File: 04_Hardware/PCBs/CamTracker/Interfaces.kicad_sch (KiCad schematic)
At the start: 58 parts, among them J7 22-28-4044, J8 22-28-4044, Q1 BC817-40,215, Q2 BC817-40,215, Q3 BC817-40,215, Q4 BC817-40,215, Q5 BC817-40,215, Q6 BC817-40,215, Q7 BC817-40,215, Q8 BC817-40,215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

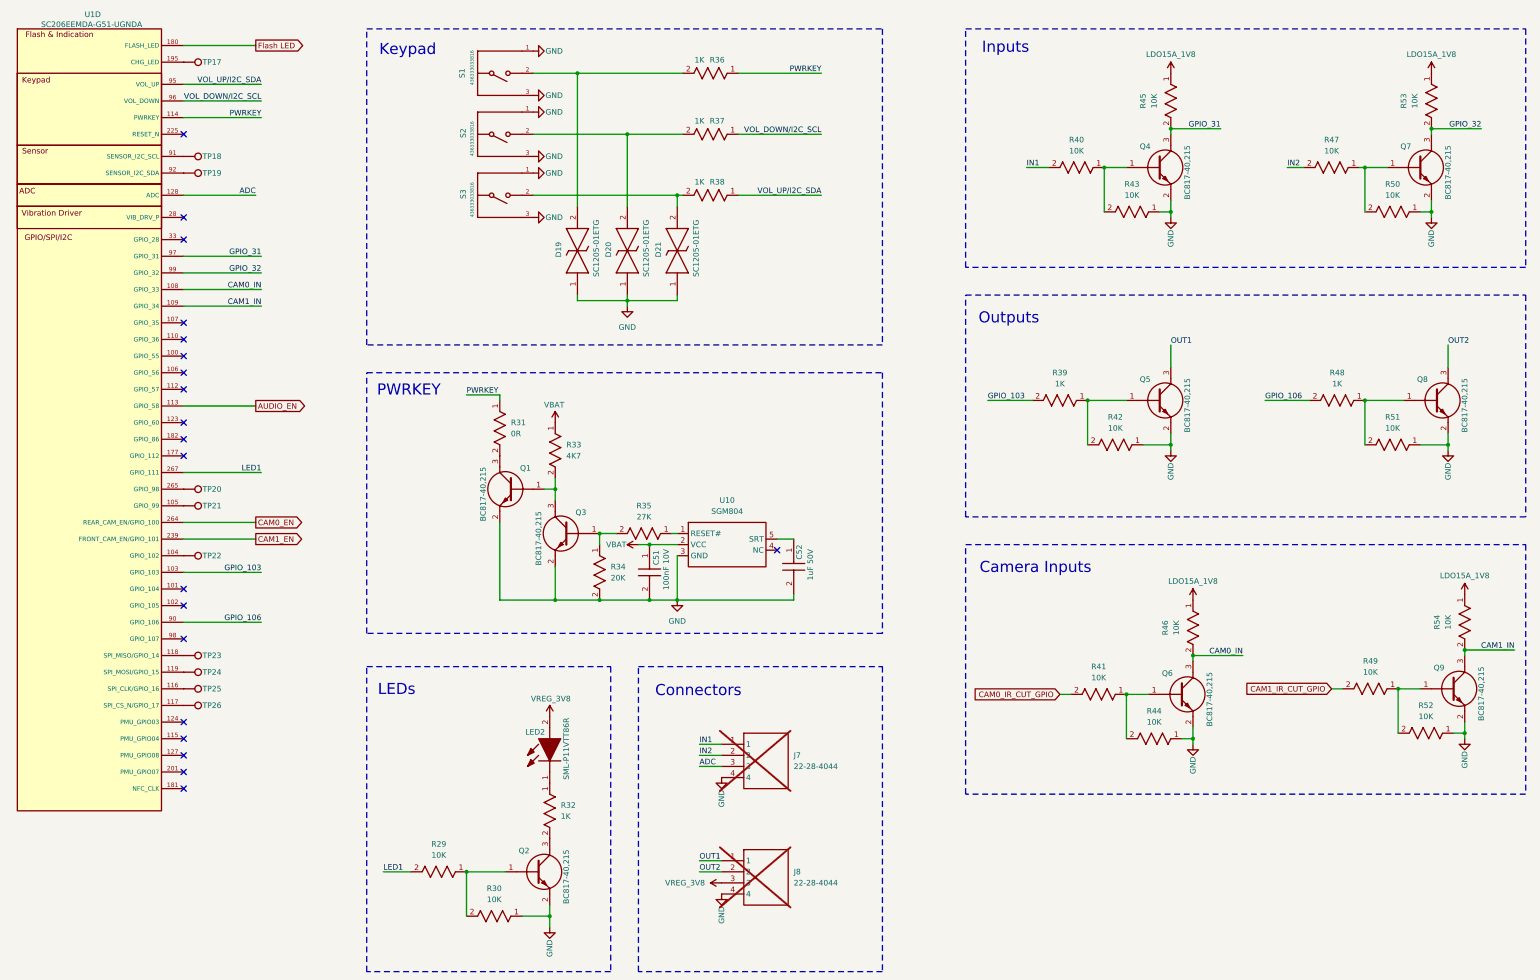
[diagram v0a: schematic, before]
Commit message: feat: Completed Placement v1 in Layout
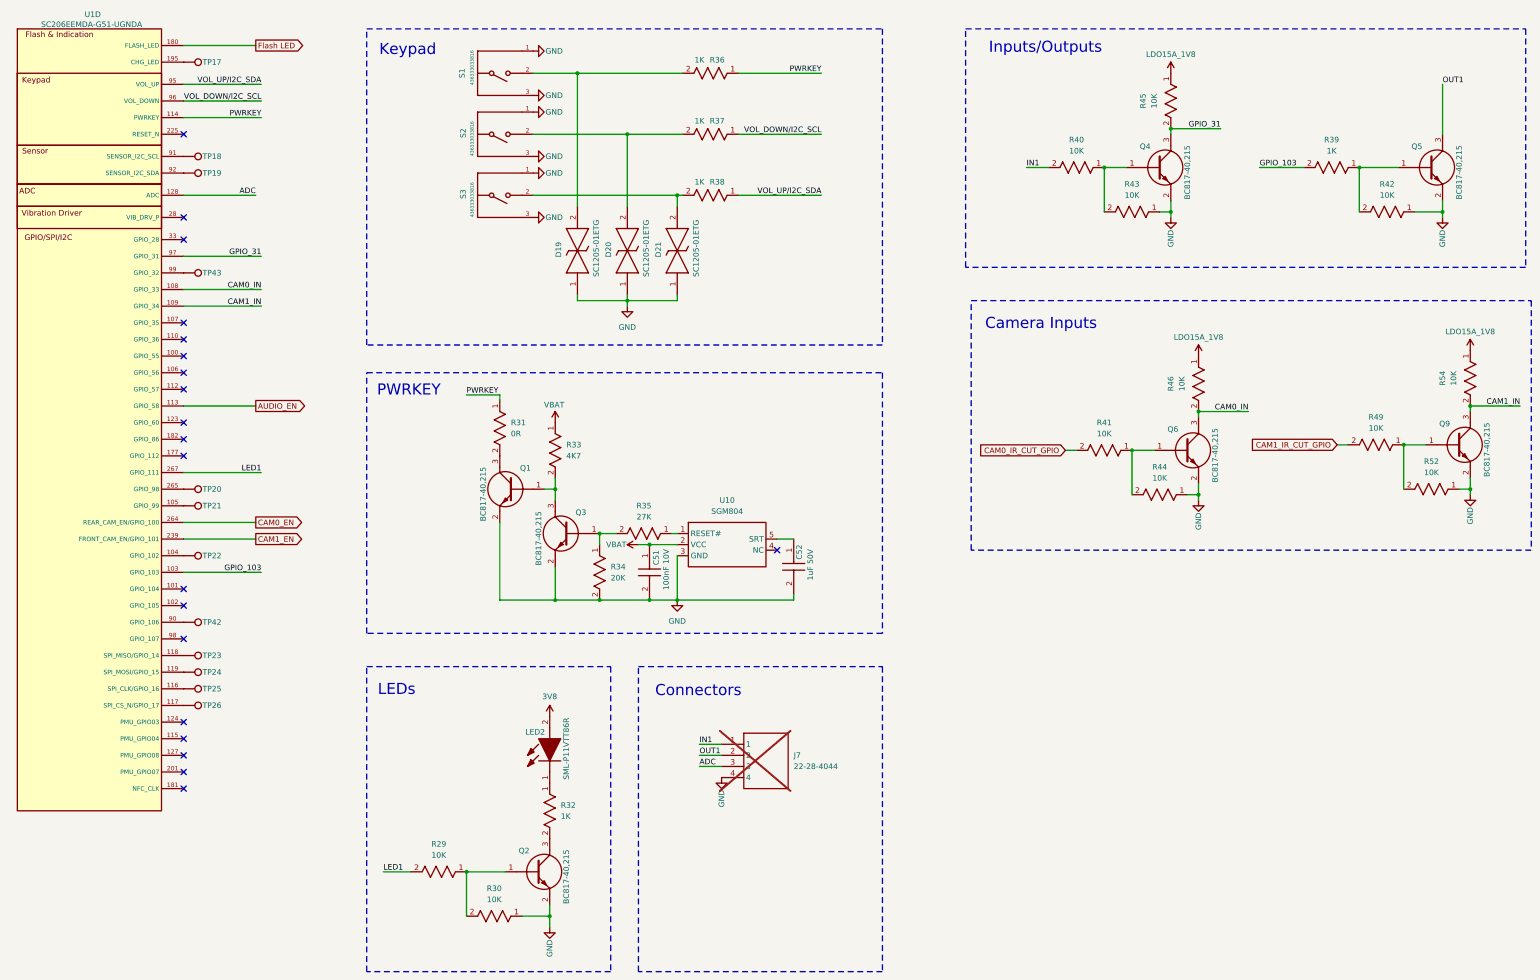
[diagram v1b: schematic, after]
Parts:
- removed J8: 22-28-4044, 000MCLib:HDRV3W66P0X254_1X4_762X249X1042P, symbol 000MCLib:22-28-4044
- removed Q7, Q8: BC817-40,215, 000MCLib:BC81740215, symbol 000MCLib:BC817-40,215
- removed R47, R50, R51, R53: 10K, 000MCLib:RC0402N_YAG, symbol 000MCLib:RC0402JR-0710KL
- removed R48: 1K, 000MCLib:RC0402N_YAG, symbol 000MCLib:RC0402JR-071KL
- added TP42, TP43: TestPoint, TestPoint:TestPoint_Pad_D1.0mm, symbol 000MCLib:TestPoint
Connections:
- net IN2 is gone; now on net OUT1: J7.2
- net GPIO_106: no longer names the net of U1.90 (GPIO_106)
- net GPIO_106: now also TP42.1
- net GPIO_32: no longer names the net of U1.99 (GPIO_32)
- net GPIO_32: now also TP43.1
- net VREG_3V8 renamed 3V8
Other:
- note added: "Inputs/Outputs"
- note removed: "Inputs"
- note removed: "Outputs"
- moved on the sheet: Q5, Q6, Q9, R39, R41, R42, R44, R46, R49, R52, R54

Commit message: feat(PCB): Finalized design and generated Gerber files and BOM
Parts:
- U10: Part Name SGM804-2.93YN5G/TR -> (none); Part Number (none) -> SGM804-2.93YN5G/TR

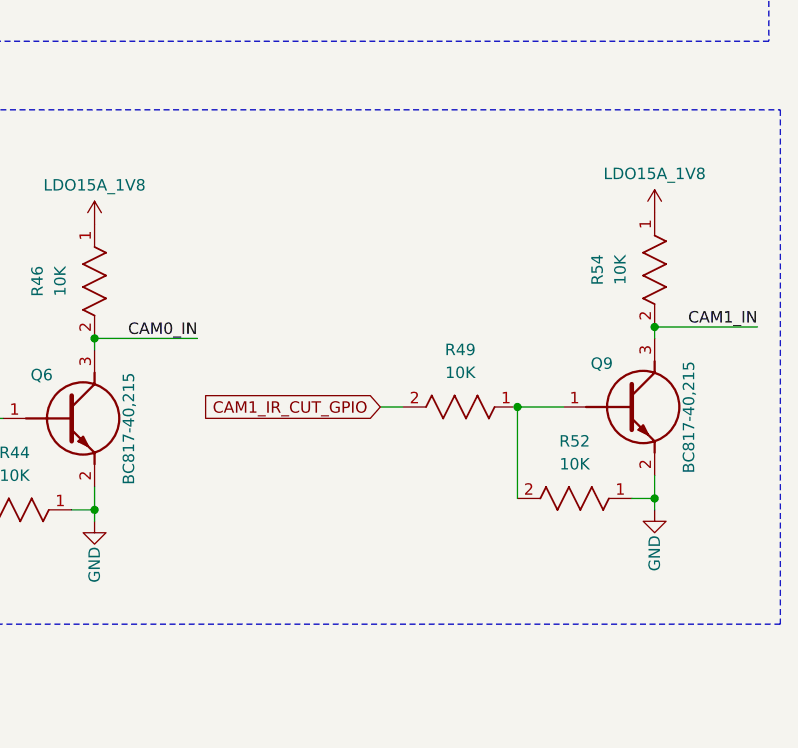
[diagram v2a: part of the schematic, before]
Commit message: feat(PCB): Cam Connectors have been changed with 2x10P
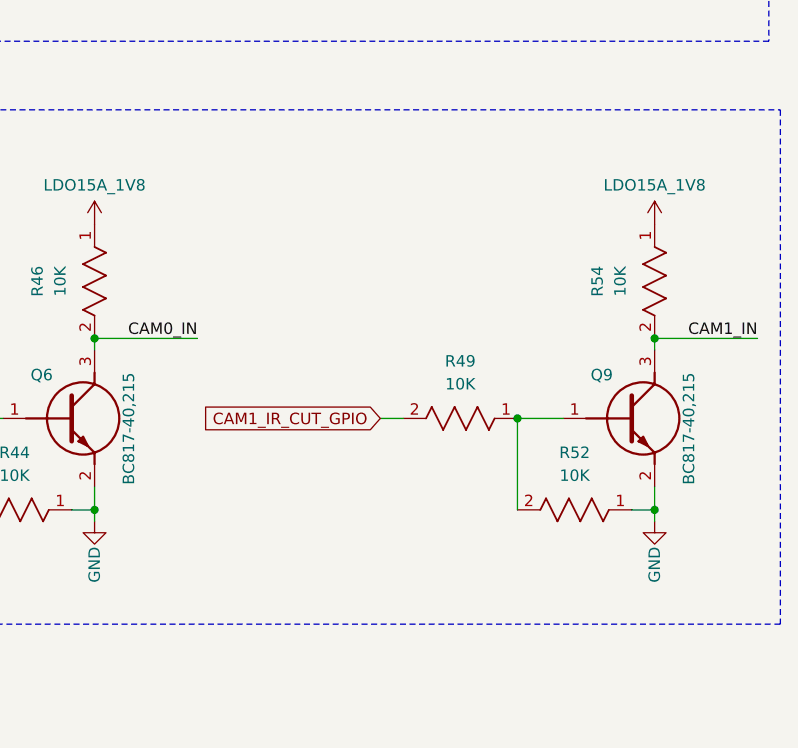
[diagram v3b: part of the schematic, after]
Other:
- moved on the sheet: Q9, R49, R52, R54

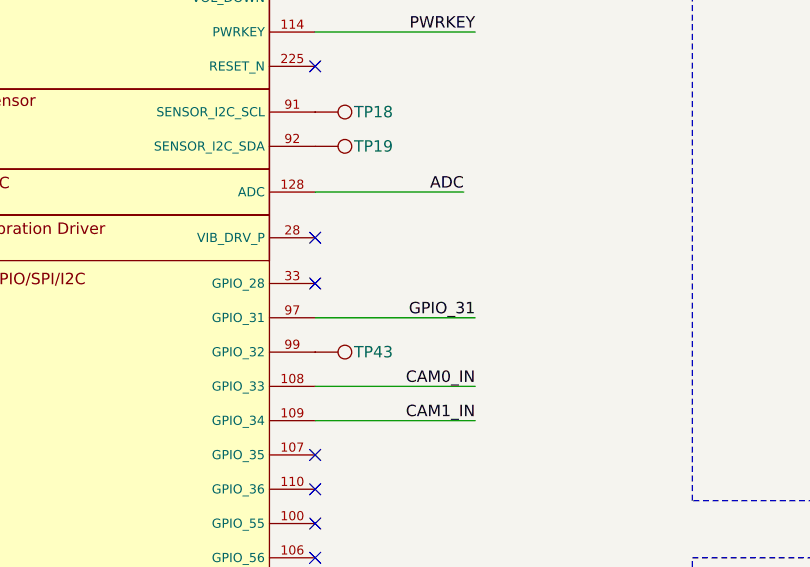
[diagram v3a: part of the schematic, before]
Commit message: feat(PCB): Added GPIO IN to SC206E from the MCU
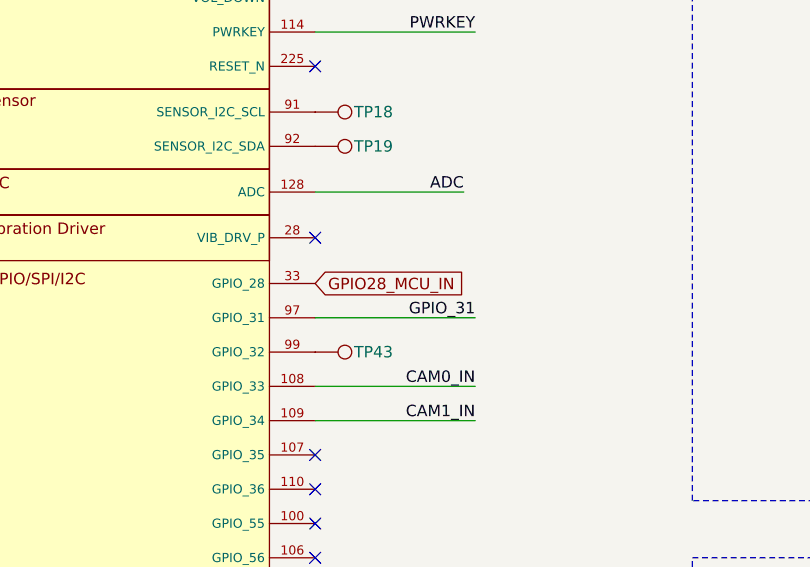
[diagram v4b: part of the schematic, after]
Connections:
- net GPIO28_MCU_IN: now reaches U1.33 (GPIO_28)
- no-connect marks 20 -> 19
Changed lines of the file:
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@@
-	)
-	(no_connect
-		(at 68.58 76.2)
 	)
 	(no_connect
@@
 				(hide yes)
 			)
+		)
+	)
+	(global_label "GPIO28_MCU_IN"
+		(shape input)
+		(at 68.58 76.2 0)
+		(fields_autoplaced yes)
+		(effects
+			(font
+				(size 1.27 1.27)
+			)
+			(justify left)
+		)
+		(property "Intersheetrefs" "${INTERSHEET_REFS}"
+			(at 86.3819 76.2 0)
+			(effects
+				(font
+					(size 1.27 1.27)
+				)
+				(justify left)
+				(hide yes)
+			)

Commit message: feat(PCB): finalize PCB design and generate BOM/Gerbers
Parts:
- R31: Height 0.5 -> (none); Mouser Part Number 71-CRCW0805-0-E3 -> (none); Mouser Price/Stock https://www.mouser.co.uk/ProductDetail/Vishay-Dale/CRCW0805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 -> (none)
